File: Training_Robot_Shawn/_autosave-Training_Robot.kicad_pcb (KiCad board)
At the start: 2 copper layers, 101.5 x 70 mm, 16 parts, among them J1 Arduino connector, J4 3V, J5 GND, M1 FrontL, M2 FrontR, M3 BackL, M4 BackR, SW1 SW_SPDT_312

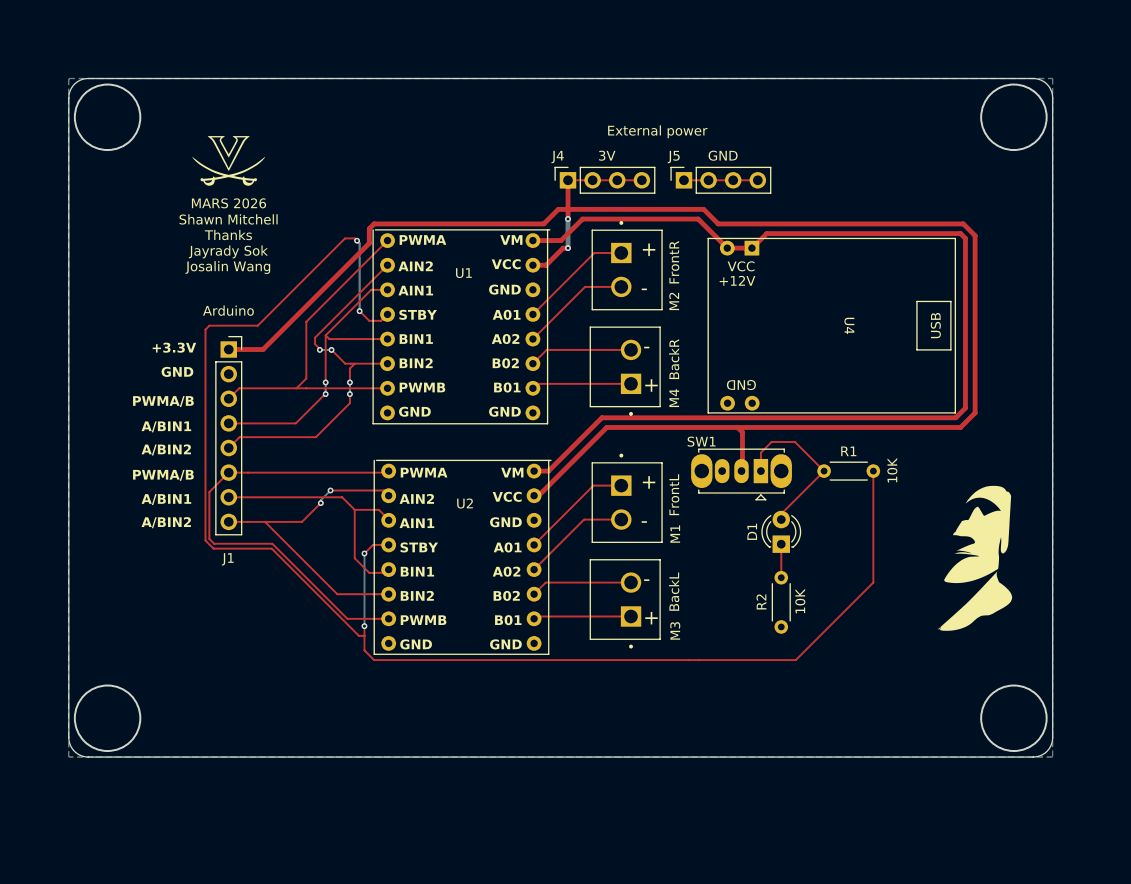
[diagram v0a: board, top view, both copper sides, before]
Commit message: Updated folder
Changed mounting hole distance
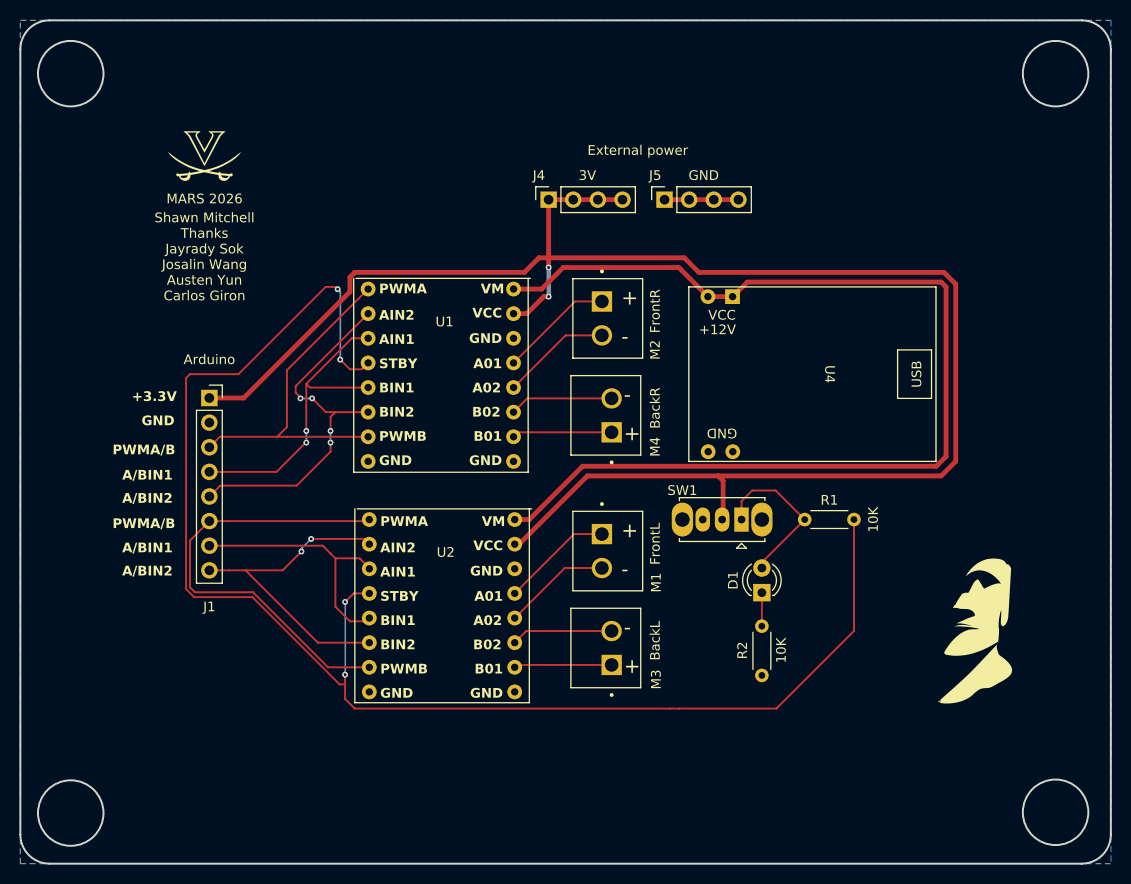
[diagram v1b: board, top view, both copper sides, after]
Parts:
- moved G*** 7.50 mm to (233.0, 92.0)
- moved D1 5.39 mm to (211.0, 88.0)
- moved M1 5.39 mm to (194.5, 82.0)
- moved M2 5.39 mm to (194.5, 58.0)
- moved M3 5.39 mm to (195.5, 95.5)
- moved M4 5.39 mm to (195.5, 71.5)
- moved R1 5.39 mm to (215.4, 80.5)
- moved R2 5.39 mm to (211.0, 96.6)
- moved SW1 5.39 mm to (208.9, 80.5)
- moved U1 5.39 mm to (178.0, 61.8)
- moved U2 5.39 mm to (178.1, 85.6)
- moved U4 5.39 mm to (221.0, 65.5)
- moved J1 5.39 mm to (154.0, 68.0)
- moved J4 2.83 mm to (189.0, 47.5)
- moved J5 2.83 mm to (201.0, 47.5)
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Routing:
- net +3V3: track 176.0 -> 179.0 mm
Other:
- board size 101.5 x 70 mm -> 112.5 x 87 mm
- board text added: "Shawn Mitchell Thanks Jayrady Sok Josalin Wang Austen Yun Carlos Giron"
- board text removed: "Shawn Mitchell Thanks Jayrady Sok Josalin Wang"
